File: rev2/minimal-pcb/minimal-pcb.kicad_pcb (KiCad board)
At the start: 2 copper layers, 70 x 75 mm, 8 parts, among them J1 USB_C_Receptacle_USB2.0

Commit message: chore: update all symbols + footprints to match kicad 8
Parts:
- MX1, MX2, MX3: footprint PCM_marbastlib-mx:SW_MX_HS_1u -> PCM_marbastlib-mx:SW_MX_HS_CPG151101S11_1u
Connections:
- J1 pad A1: Net-(J1-GND-PadA1) -> unconnected-(J1-GND-PadA1)_1
- J1 pad A12: Net-(J1-GND-PadA1) -> unconnected-(J1-GND-PadA1)_0
- J1 pad A4: Net-(J1-VBUS-PadA4) -> unconnected-(J1-VBUS-PadA4)_0
- J1 pad A8: unconnected-(J1-SBU1-PadA8) -> (no net)
- J1 pad A9: Net-(J1-VBUS-PadA4) -> unconnected-(J1-VBUS-PadA4)_1
- J1 pad B1: Net-(J1-GND-PadA1) -> unconnected-(J1-GND-PadA1)
- J1 pad B12: Net-(J1-GND-PadA1) -> unconnected-(J1-GND-PadA1)_2
- J1 pad B4: Net-(J1-VBUS-PadA4) -> unconnected-(J1-VBUS-PadA4)
- J1 pad B8: unconnected-(J1-SBU2-PadB8) -> (no net)
- J1 pad B9: Net-(J1-VBUS-PadA4) -> unconnected-(J1-VBUS-PadA4)_2

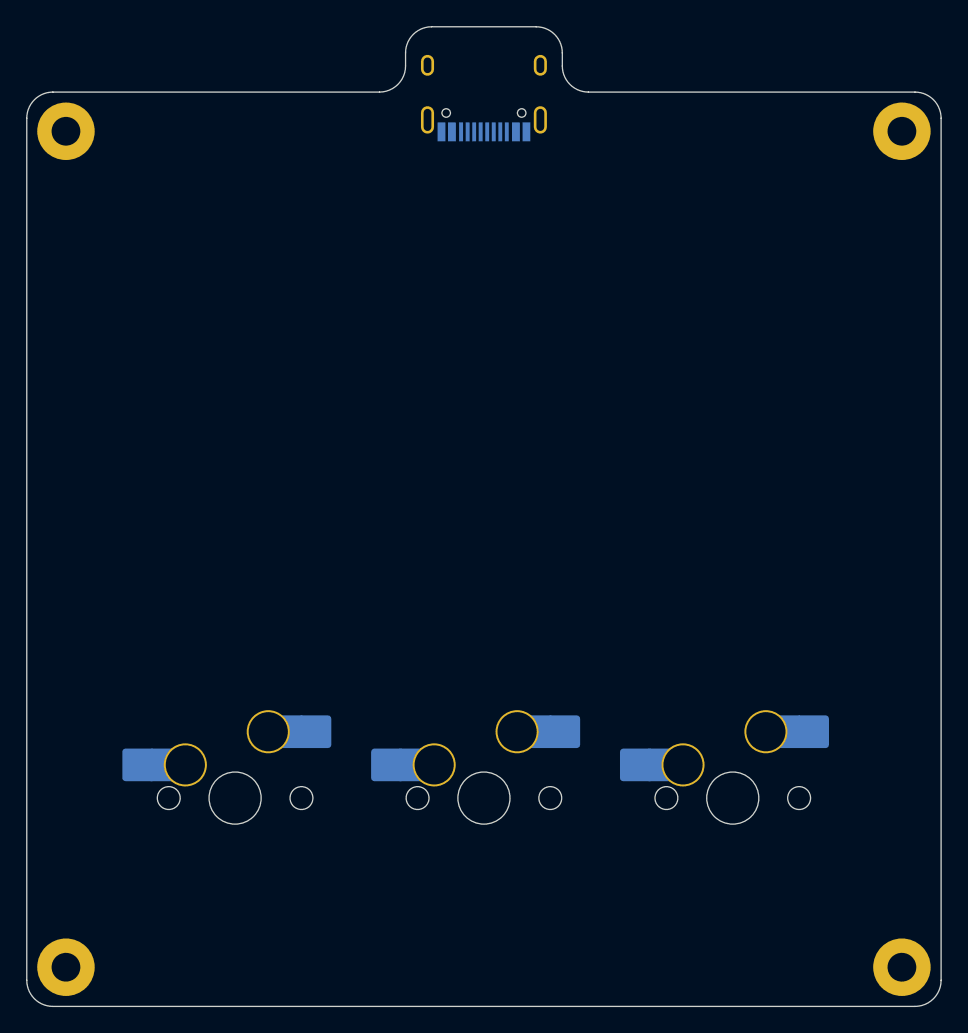
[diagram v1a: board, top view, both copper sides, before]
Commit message: feat: initial attempt at new case
shrinking it is a bit difficult without knowing what's on the PCB - need to make sure I can route this...

probably better to design the PCB first so I know what the minimum size is.
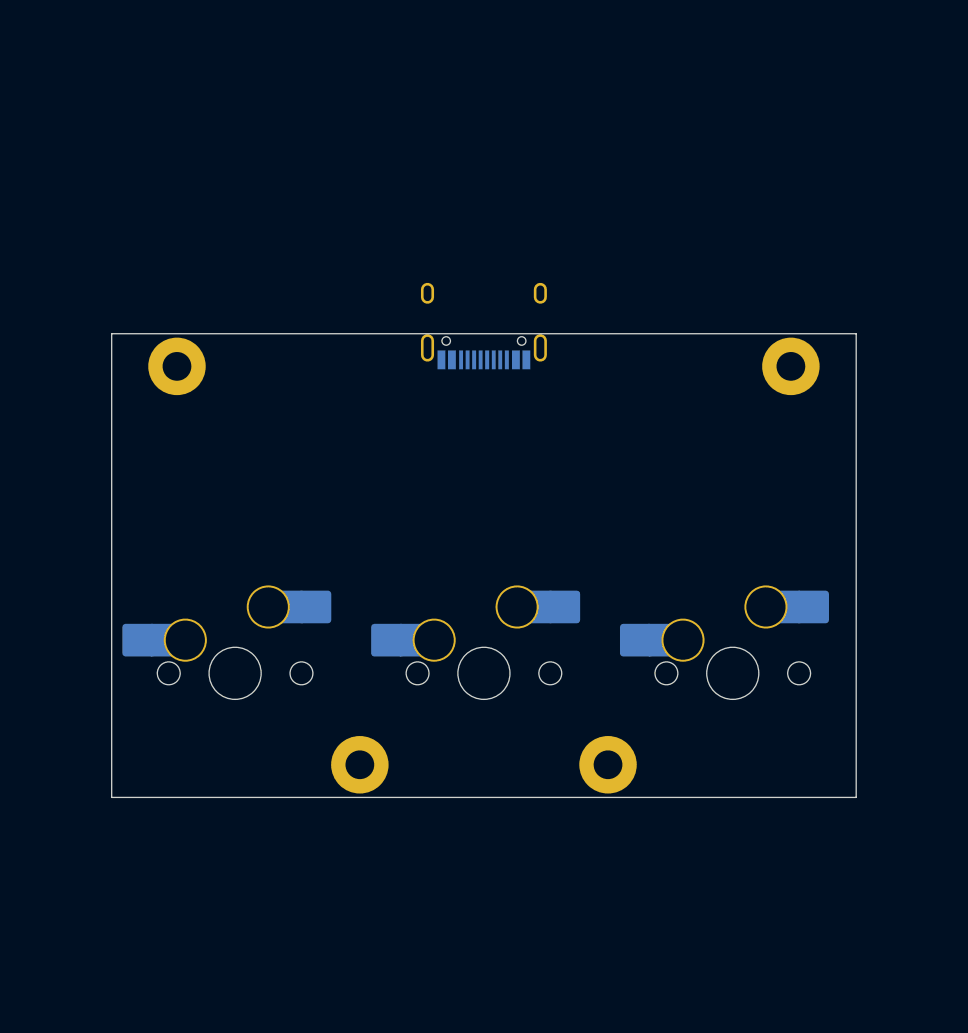
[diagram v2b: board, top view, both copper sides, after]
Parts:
- moved H3 27.3 mm to (47.6, 73.3)
- moved H4 27.3 mm to (66.7, 73.3)
- moved H1 19.9 mm to (33.6, 42.8)
- moved H2 19.9 mm to (80.7, 42.8)
- moved J1 17.5 mm to (57.1, 38.2)
- moved MX1 9.55 mm to (76.2, 66.3)
- moved MX2 9.55 mm to (57.1, 66.3)
- moved MX3 9.55 mm to (38.1, 66.3)
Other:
- board size 70 x 75 mm -> 57 x 35.5 mm
- board text added: "60x45mm Case ??x??mm PCB ??mm extension at top of PCB for USB-C port Switches ??mm below centre of PCB M2 mounting holes ??mm away from edge"
- board text removed: "70x70mm PCB 5mm extension at top of PCB for USB-C port Switches 19.05mm below centre of PCB M2 mounting holes 3mm away from edge"
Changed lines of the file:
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@@
 	(footprint "PCM_marbastlib-mx:SW_MX_HS_CPG151101S11_1u"
 		(layer "B.Cu")
-		(at 38.099984 75.811647 180)
+		(at 38.099984 66.261647 180)
 		(descr "Footprint for Cherry MX style switches with Kailh hotswap socket")
 		(property "Reference" "MX3"
@@
 				(font
 					(size 1.27 1.27)
+					(thickness 0.15)
 				)
 				(justify mirror)
@@
 				(font
 					(size 1.27 1.27)
+					(thickness 0.15)
 				)
 				(justify mirror)
@@
 				(font
 					(size 1.27 1.27)
+					(thickness 0.15)
 				)
 				(justify mirror)
@@
 	(footprint "PCM_marbastlib-mx:SW_MX_HS_CPG151101S11_1u"
 		(layer "B.Cu")
-		(at 57.15 75.811647 180)
+		(at 57.15 66.261647 180)
 		(descr "Footprint for Cherry MX style switches with Kailh hotswap socket")
 		(property "Reference" "MX2"
@@
 				(font
 					(size 1.27 1.27)
+					(thickness 0.15)
 				)
 				(justify mirror)
@@
 				(font
 					(size 1.27 1.27)
+					(thickness 0.15)
 				)
 				(justify mirror)
@@
 				(font
 					(size 1.27 1.27)
+					(thickness 0.15)
 				)
 				(justify mirror)
@@
 		(fp_arc
 			(start 6.085176 4.75022)
-			(mid 5.499389 6.164432)
+			(mid 5.499388 6.164432)
 			(end 4.085176 6.75022)
 			(stroke
@@
 		(fp_arc
 			(start 6.085176 4.75022)
-			(mid 5.499389 6.164432)
+			(mid 5.499388 6.164432)
 			(end 4.085176 6.75022)
 			(stroke
@@
 		(fp_arc
 			(start 6.085176 4.75022)
-			(mid 5.499389 6.164432)
+			(mid 5.499388 6.164432)
 			(end 4.085176 6.75022)
 			(stroke
@@
 	(footprint "PCM_marbastlib-mx:SW_MX_HS_CPG151101S11_1u"
 		(layer "B.Cu")
-		(at 76.200016 75.811647 180)
+		(at 76.200016 66.261647 180)
 		(descr "Footprint for Cherry MX style switches with Kailh hotswap socket")
 		(property "Reference" "MX1"
@@
 				(font
 					(size 1.27 1.27)
+					(thickness 0.15)
 				)
 				(justify mirror)
@@
 				(font
 					(size 1.27 1.27)
+					(thickness 0.15)
 				)
 				(justify mirror)
@@
 				(font
 					(size 1.27 1.27)
+					(thickness 0.15)
 				)
 				(justify mirror)
@@
 	(footprint "MountingHole:MountingHole_2.2mm_M2_Pad"
 		(layer "B.Cu")
-		(at 89.15 24.761647 180)
+		(at 80.65 42.761647 180)
 		(descr "Mounting Hole 2.2mm, M2")
 		(tags "mounting hole 2.2mm m2")
@@
 				(font
 					(size 1.27 1.27)
+					(thickness 0.15)
 				)
 			)
@@
 				(font
 					(size 1.27 1.27)
+					(thickness 0.15)
 				)
 			)
@@
 				(font
 					(size 1.27 1.27)
+					(thickness 0.15)
 				)
 			)
@@
 	(footprint "MountingHole:MountingHole_2.2mm_M2_Pad"
 		(layer "B.Cu")
-		(at 89.15 88.761647 180)
+		(at 66.65 73.261647 180)
 		(descr "Mounting Hole 2.2mm, M2")
 		(tags "mounting hole 2.2mm m2")
@@
 				(font
 					(size 1.27 1.27)
+					(thickness 0.15)
 				)
 			)
@@
 				(font
 					(size 1.27 1.27)
+					(thickness 0.15)
 				)
 			)
@@
 				(font
 					(size 1.27 1.27)
+					(thickness 0.15)
 				)
 			)
@@
 	(footprint "MountingHole:MountingHole_2.2mm_M2_Pad"
 		(layer "B.Cu")
-		(at 25.15 88.761647 180)
+		(at 47.65 73.261647 180)
 		(descr "Mounting Hole 2.2mm, M2")
 		(tags "mounting hole 2.2mm m2")
@@
 				(font
 					(size 1.27 1.27)
+					(thickness 0.15)
 				)
 			)
@@
 				(font
 					(size 1.27 1.27)
+					(thickness 0.15)
 				)
 			)
@@
 				(font
 					(size 1.27 1.27)
+					(thickness 0.15)
 				)
 			)
@@
 	(footprint "MountingHole:MountingHole_2.2mm_M2_Pad"
 		(layer "B.Cu")
-		(at 25.15 24.761647 180)
+		(at 33.65 42.761647 180)
 		(descr "Mounting Hole 2.2mm, M2")
 		(tags "mounting hole 2.2mm m2")
@@
 				(font
 					(size 1.27 1.27)
+					(thickness 0.15)
 				)
 			)
@@
 				(font
 					(size 1.27 1.27)
+					(thickness 0.15)
 				)
 			)
@@
 				(font
 					(size 1.27 1.27)
+					(thickness 0.15)
 				)
 			)
@@
 	(footprint "PCM_marbastlib-various:USB_C_Receptacle_HRO_TYPE-C-31-M-12"
 		(layer "B.Cu")
-		(at 57.15 20.761647)
+		(at 57.15 38.216647)
 		(descr "USB Type-C receptacle for USB 2.0 and PD, http://www.krhro.com/uploads/soft/180320/1-1P320120243.pdf")
 		(tags "usb usb-c 2.0 pd")
@@
 				(font
 					(size 1.27 1.27)
+					(thickness 0.15)
 				)
 			)
@@
 				(font
 					(size 1.27 1.27)
+					(thickness 0.15)
 				)
 			)
@@
 				(font
 					(size 1.27 1.27)
+					(thickness 0.15)
 				)
 			)
@@
 		)
 	)
-	(gr_line
-		(start 24.15 21.761647)
-		(end 49.15 21.761647)
+	(gr_rect
+		(start 27.15 34.261647)
+		(end 87.15 79.261647)
+		(stroke
+			(width 0.1)
+			(type dash)
+		)
+		(fill none)
+		(layer "Dwgs.User")
+	)
+	(gr_rect
+		(start 28.65 40.261647)
+		(end 85.65 75.761647)
 		(stroke
 			(width 0.1)
 			(type default)
 		)
+		(fill none)
 		(layer "Edge.Cuts")
 	)
-	(gr_arc
-		(start 92.15 89.761647)
-		(mid 91.564197 91.17583)
-		(end 90.15 91.761647)
-		(stroke
-			(width 0.1)
-			(type default)
-		)
-		(layer "Edge.Cuts")
-	)
-	(gr_line
-		(start 65.15 21.761647)
-		(end 90.15 21.761647)
-		(stroke
-			(width 0.1)
-			(type default)
-		)
-		(layer "Edge.Cuts")
-	)
-	(gr_line
-		(start 63.15 18.761647)
-		(end 63.15 19.761647)
-		(stroke
-			(width 0.1)
-			(type default)
-		)
-		(layer "Edge.Cuts")
-	)
-	(gr_arc
-		(start 51.15 19.761647)
-		(mid 50.564197 21.17583)
-		(end 49.15 21.761647)
-		(stroke
-			(width 0.1)
-			(type default)
-		)
-		(layer "Edge.Cuts")
-	)
-	(gr_arc
-		(start 22.15 23.761647)
-		(mid 22.73577 22.347403)
-		(end 24.15 21.761647)
-		(stroke
-			(width 0.1)
-			(type default)
-		)
-		(layer "Edge.Cuts")
-	)
-	(gr_line
-		(start 90.15 91.761647)
-		(end 24.15 91.761647)
-		(stroke
-			(width 0.1)
-			(type default)
-		)
-		(layer "Edge.Cuts")
-	)
-	(gr_arc
-		(start 51.15 18.761647)
-		(mid 51.73577 17.347403)
-		(end 53.15 16.761647)
-		(stroke
-			(width 0.1)
-			(type default)
-		)
-		(layer "Edge.Cuts")
-	)
-	(gr_arc
-		(start 61.15 16.761647)
-		(mid 62.564214 17.347433)
-		(end 63.15 18.761647)
-		(stroke
-			(width 0.1)
-			(type default)
-		)
-		(layer "Edge.Cuts")
-	)
-	(gr_line
-		(start 22.15 89.761647)
-		(end 22.15 23.761647)
-		(stroke
-			(width 0.1)
-			(type default)
-		)
-		(layer "Edge.Cuts")
-	)
-	(gr_arc
-		(start 24.15 91.761647)
-		(mid 22.735786 91.175861)
-		(end 22.15 89.761647)
-		(stroke
-			(width 0.1)
-			(type default)
-		)
-		(layer "Edge.Cuts")
-	)
-	(gr_line
-		(start 92.15 23.761647)
-		(end 92.15 89.761647)
-		(stroke
-			(width 0.1)
-			(type default)
-		)
-		(layer "Edge.Cuts")
-	)
-	(gr_line
-		(start 53.15 16.761647)
-		(end 61.15 16.761647)
-		(stroke
-			(width 0.1)
-			(type default)
-		)
-		(layer "Edge.Cuts")
-	)
-	(gr_arc
-		(start 65.15 21.761647)
-		(mid 63.735786 21.175861)
-		(end 63.15 19.761647)
-		(stroke
-			(width 0.1)
-			(type default)
-		)
-		(layer "Edge.Cuts")
-	)
-	(gr_line
-		(start 51.15 19.761647)
-		(end 51.15 18.761647)
-		(stroke
-			(width 0.1)
-			(type default)
-		)
-		(layer "Edge.Cuts")
-	)
-	(gr_arc
-		(start 90.15 21.761647)
-		(mid 91.564214 22.347433)
-		(end 92.15 23.761647)
-		(stroke
-			(width 0.1)
-			(type default)
-		)
-		(layer "Edge.Cuts")
-	)
-	(gr_text "70x70mm PCB\n5mm extension at top of PCB for USB-C port\nSwitches 19.05mm below centre of PCB\nM2 mounting holes 3mm away from edge"
-		(at 97.15 27.761647 0)
+	(gr_text "60x45mm Case\n??x??mm PCB\n??mm extension at top of PCB for USB-C port\nSwitches ??mm below centre of PCB\nM2 mounting holes ??mm away from edge"
+		(at 88.15 41.761647 0)
 		(layer "Cmts.User")
 		(effects
